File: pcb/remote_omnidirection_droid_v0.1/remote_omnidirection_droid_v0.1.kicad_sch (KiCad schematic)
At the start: 30 parts, among them J1 USB_C_Receptacle_USB2.0, J4 Conn_01x02, Q1 BC846BS, SW1 SW_SPST, U1 USBLC6-2SC6, U3 AZ1117-3.3, U4 AZ1117-5.0, U5 ESP32-S3-WROOM-2-N32R8V

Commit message: poorly designed a PCB
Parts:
- C11, C12, C17: footprint (none) -> Capacitor_SMD:C_1206_3216Metric_Pad1.33x1.80mm_HandSolder
- D1, D2, D8, D9: footprint (none) -> LED_SMD:LED_1206_3216Metric_Pad1.42x1.75mm_HandSolder
- D3, D7: footprint (none) -> Diode_SMD:D_1206_3216Metric_Pad1.42x1.75mm_HandSolder
- J4: footprint (none) -> TestPoint:TestPoint_2Pads_Pitch5.08mm_Drill1.3mm
- R10, R11, R5, R6, R7, R8: footprint (none) -> Resistor_SMD:R_1206_3216Metric_Pad1.30x1.75mm_HandSolder
- U5: footprint ESP32-S3-WROOM-2-N32R8V:XCVR_ESP32-S3-WROOM-2-N32R8V -> ESP32 S3:XCVR_ESP32-S3-WROOM-2-N32R8V
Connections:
- net IO0: no longer names the net of U5.27 (IO0)
- no-connect marks 7 -> 33
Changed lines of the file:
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@@
   (junction (at 56.515 132.715) (diameter 0) (color 0 0 0 0)
   )
+  (no_connect (at 165.1 160.02))
+  (no_connect (at 195.58 167.64))
+  (no_connect (at 195.58 165.1))
+  (no_connect (at 195.58 157.48))
+  (no_connect (at 165.1 162.56))
+  (no_connect (at 165.1 167.64))
   (no_connect (at 165.1 137.16))
+  (no_connect (at 165.1 147.32))
+  (no_connect (at 195.58 162.56))
+  (no_connect (at 165.1 144.78))
+  (no_connect (at 165.1 180.34))
+  (no_connect (at 195.58 142.24))
+  (no_connect (at 165.1 177.8))
+  (no_connect (at 195.58 170.18))
   (no_connect (at 64.135 75.565))
+  (no_connect (at 195.58 147.32))
   (no_connect (at 195.58 175.26))
+  (no_connect (at 165.1 152.4))
+  (no_connect (at 195.58 144.78))
+  (no_connect (at 165.1 170.18))
   (no_connect (at 195.58 177.8))
   (no_connect (at 165.1 134.62))
+  (no_connect (at 165.1 175.26))
+  (no_connect (at 195.58 160.02))
+  (no_connect (at 195.58 154.94))
+  (no_connect (at 165.1 172.72))
   (no_connect (at 165.1 149.86))
+  (no_connect (at 195.58 172.72))
+  (no_connect (at 165.1 154.94))
+  (no_connect (at 165.1 157.48))
   (no_connect (at 64.135 73.025))
+  (no_connect (at 165.1 142.24))
+  (no_connect (at 165.1 165.1))
   (wire (pts (xy 83.185 187.325) (xy 94.615 187.325))
     (stroke (width 0) (type default))
@@
     (stroke (width 0) (type default))
   )
-  (wire (pts (xy 161.29 142.24) (xy 165.1 142.24))
-    (stroke (width 0) (type default))
-  )
   (wire (pts (xy 31.75 215.9) (xy 38.735 215.9))
     (stroke (width 0) (type default))
@@
     (stroke (width 0) (type default))
   )
-  (text_box "ESP32-S3-WROOM Module"
-    (at 125.095 98.425 0) (size 111.125 106.045)
+  (text_box "Enable/Reset Switch"
+    (at 13.335 204.47 0) (size 45.72 27.305)
     (stroke (width 0) (type default))
     (fill (type none))
     (effects (font (size 1.27 1.27)) (justify left top))
   )
-  (text_box "Enable/Reset Switch"
-    (at 13.335 204.47 0) (size 45.72 27.305)
+  (text_box "Power Management"
+    (at 13.335 98.425 0) (size 111.76 106.045)
     (stroke (width 0) (type default))
     (fill (type none))
     (effects (font (size 1.27 1.27)) (justify left top))
   )
-  (text_box "Power Management"
-    (at 13.335 98.425 0) (size 111.76 106.045)
+  (text_box "USB-C + ESD Protection"
+    (at 13.335 34.29 0) (size 111.76 64.135)
     (stroke (width 0) (type default))
     (fill (type none))
     (effects (font (size 1.27 1.27)) (justify left top))
   )
-  (text_box "USB-C + ESD Protection"
-    (at 13.335 34.29 0) (size 111.76 64.135)
+  (text_box "Power Flags"
+    (at 13.335 13.335 0) (size 111.76 20.955)
     (stroke (width 0) (type default))
     (fill (type none))
     (effects (font (size 1.27 1.27)) (justify left top))
   )
-  (text_box "Power Flags"
-    (at 13.335 13.335 0) (size 111.76 20.955)
-    (stroke (width 0) (type default))
-    (fill (type none))
-    (effects (font (size 1.27 1.27)) (justify left top))
-  )
   (label "LED_BATT" (at 83.185 187.325 0) (fields_autoplaced)
     (effects (font (size 1.27 1.27)) (justify left bottom))
@@
     (effects (font (size 1.27 1.27)) (justify left bottom))
   )
-  (label "IO0" (at 161.29 142.24 0) (fields_autoplaced)
-    (effects (font (size 1.27 1.27)) (justify left bottom))
-  )
   (label "EN" (at 52.705 215.9 180) (fields_autoplaced)
     (effects (font (size 1.27 1.27)) (justify right bottom))
@@
       (effects (font (size 1.27 1.27)))
     )
-    (property "Footprint" "ESP32-S3-WROOM-2-N32R8V:XCVR_ESP32-S3-WROOM-2-N32R8V" (at 180.34 157.48 0)
+    (property "Footprint" "ESP32 S3:XCVR_ESP32-S3-WROOM-2-N32R8V" (at 180.34 157.48 0)
       (effects (font (size 1.27 1.27)) (justify bottom) hide)
     )
@@
       (effects (font (size 1.27 1.27)))
     )
-    (property "Footprint" "" (at 81.915 164.465 0)
+    (property "Footprint" "Resistor_SMD:R_1206_3216Metric_Pad1.30x1.75mm_HandSolder" (at 81.915 164.465 0)
       (effects (font (size 1.27 1.27)) hide)
     )
@@
       (effects (font (size 1.27 1.27)))
     )
-    (property "Footprint" "" (at 93.345 158.115 0)
+    (property "Footprint" "LED_SMD:LED_1206_3216Metric_Pad1.42x1.75mm_HandSolder" (at 93.345 158.115 0)
       (effects (font (size 1.27 1.27)) hide)
     )
@@
       (effects (font (size 1.27 1.27)))
     )
-    (property "Footprint" "" (at 30.48 132.715 0)
+    (property "Footprint" "Diode_SMD:D_1206_3216Metric_Pad1.42x1.75mm_HandSolder" (at 30.48 132.715 0)
       (effects (font (size 1.27 1.27)) hide)
     )
@@
       (effects (font (size 1.27 1.27)))
     )
-    (property "Footprint" "" (at 81.915 151.765 0)
+    (property "Footprint" "Resistor_SMD:R_1206_3216Metric_Pad1.30x1.75mm_HandSolder" (at 81.915 151.765 0)
       (effects (font (size 1.27 1.27)) hide)
     )
@@
       (effects (font (size 1.27 1.27)))
     )
-    (property "Footprint" "" (at 62.23 132.715 0)
+    (property "Footprint" "Diode_SMD:D_1206_3216Metric_Pad1.42x1.75mm_HandSolder" (at 62.23 132.715 0)
       (effects (font (size 1.27 1.27)) hide)
     )
@@
       (effects (font (size 1.27 1.27)))
     )
-    (property "Footprint" "" (at 93.345 145.415 0)
+    (property "Footprint" "LED_SMD:LED_1206_3216Metric_Pad1.42x1.75mm_HandSolder" (at 93.345 145.415 0)
       (effects (font (size 1.27 1.27)) hide)
     )
@@
       (effects (font (size 1.27 1.27)))
     )
-    (property "Footprint" "" (at 180.34 114.3 0)
+    (property "Footprint" "Resistor_SMD:R_1206_3216Metric_Pad1.30x1.75mm_HandSolder" (at 180.34 114.3 0)
       (effects (font (size 1.27 1.27)) hide)
     )
@@
       (effects (font (size 1.27 1.27)) (justify left))
     )
-    (property "Footprint" "" (at 102.235 187.325 0)
+    (property "Footprint" "TestPoint:TestPoint_2Pads_Pitch5.08mm_Drill1.3mm" (at 102.235 187.325 0)
       (effects (font (size 1.27 1.27)) hide)
     )
@@
       (effects (font (size 1.27 1.27)))
     )
-    (property "Footprint" "" (at 81.915 145.415 0)
+    (property "Footprint" "Resistor_SMD:R_1206_3216Metric_Pad1.30x1.75mm_HandSolder" (at 81.915 145.415 0)
       (effects (font (size 1.27 1.27)) hide)
     )
@@
       (effects (font (size 1.27 1.27)) (justify left))
     )
-    (property "Footprint" "" (at 207.01 131.445 0)
+    (property "Footprint" "Capacitor_SMD:C_1206_3216Metric_Pad1.33x1.80mm_HandSolder" (at 207.01 131.445 0)
       (effects (font (size 1.27 1.27)) hide)
     )
@@
       (effects (font (size 1.27 1.27)))
     )
-    (property "Footprint" "" (at 93.345 151.765 0)
+    (property "Footprint" "LED_SMD:LED_1206_3216Metric_Pad1.42x1.75mm_HandSolder" (at 93.345 151.765 0)
       (effects (font (size 1.27 1.27)) hide)
     )
@@
       (effects (font (size 1.27 1.27)) (justify left))
     )
-    (property "Footprint" "" (at 215.265 131.445 0)
+    (property "Footprint" "Capacitor_SMD:C_1206_3216Metric_Pad1.33x1.80mm_HandSolder" (at 215.265 131.445 0)
       (effects (font (size 1.27 1.27)) hide)
     )
@@
       (effects (font (size 1.27 1.27)))
     )
-    (property "Footprint" "" (at 41.91 107.315 0)
+    (property "Footprint" "Resistor_SMD:R_1206_3216Metric_Pad1.30x1.75mm_HandSolder" (at 41.91 107.315 0)
       (effects (font (size 1.27 1.27)) hide)
     )
@@
       (effects (font (size 1.27 1.27)))
     )
-    (property "Footprint" "" (at 93.345 164.465 0)
+    (property "Footprint" "LED_SMD:LED_1206_3216Metric_Pad1.42x1.75mm_HandSolder" (at 93.345 164.465 0)
       (effects (font (size 1.27 1.27)) hide)
     )
@@
       (effects (font (size 1.27 1.27)) (justify left))
     )
-    (property "Footprint" "" (at 39.37 125.095 0)
+    (property "Footprint" "Capacitor_SMD:C_1206_3216Metric_Pad1.33x1.80mm_HandSolder" (at 39.37 125.095 0)
       (effects (font (size 1.27 1.27)) hide)
     )
@@
       (effects (font (size 1.27 1.27)))
     )
-    (property "Footprint" "" (at 81.915 158.115 0)
-      (effects (font (size 1.27 1.27)) hide)
-    )
+    (property "Footprint" "Resistor_SMD:R_1206_3216Metric_Pad1.30x1.75mm_HandSolder" (at 81.915 158.115 0)
+      (effects (font (size 1.27 1.27)) hide)
+    )

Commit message: updated PCB
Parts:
- added C4: 0.1u, Capacitor_SMD:C_1206_3216Metric_Pad1.33x1.80mm_HandSolder, symbol Device:C_Small
- added J2, J4, J5: Conn_01x04, Connector_PinSocket_2.54mm:PinSocket_1x04_P2.54mm_Vertical_SMD_Pin1Left, symbol Connector_Generic:Conn_01x04
- added M1, M2, M3: Motor_DC_ALT, pimoroni_motor_breakout:Pimoroni_Motor_Breakout, symbol Motor:Motor_DC_ALT
- added R10, R11, R12, R13, R7, R8: 10k, Resistor_SMD:R_1206_3216Metric_Pad1.30x1.75mm_HandSolder, symbol Device:R_Small_US
- added SW2: SW_SPST, Button_Switch_SMD:SW_Tactile_SPST_NO_Straight_CK_PTS636Sx25SMTRLFS, symbol Switch:SW_SPST
- added SW3: SW_SPDT, myparts:SWITCH_25336NA_APM, symbol Switch:SW_SPDT
- added TP1: AMMETER_CONN, TestPoint:TestPoint_2Pads_Pitch5.08mm_Drill1.3mm, symbol Connector:TestPoint_2Pole
- J3: renamed from J4; value Conn_01x02 -> BATT_CONNECT; footprint TestPoint:TestPoint_2Pads_Pitch5.08mm_Drill1.3mm -> myparts:Deans T-Plug Header
- renumbered C7 to C1, C9 to C2, C14 to C3, C17 to C5, C8 to C6, C10 to C7, C12 to C8, C11 to C9, D3 to D1, D8 to D3, D9 to D4, D7 to D5, D1 to D6, R10 to R14, R11 to R3, R6 to R4, R7 to R5, R8 to R6, R5 to R9, U3 to U1, U4 to U2, U1 to U3, U5 to U4
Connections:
- net +3V3: now also R4.1; no longer R5.1
- net +5V: now also R5.1, J2.1 (Pin_1), J4.1 (Pin_1), J5.1 (Pin_1); no longer R4.1
- net +BATT: now also SW3.3 (C), TP1.1; no longer J3.1 (Pin_1)
- net GND: now also C4.2, J2.4 (Pin_4), J4.4 (Pin_4), J5.4 (Pin_4), R11.2, R13.2, R8.2, SW2.1 (A)
- net BOOT: now reaches U4.27 (IO0)
- net BOOT: now also C4.1, SW2.2 (B)
- net CC1: now reaches J1.A5 (CC1), R2.2
- net NESD_D+: now reaches J1.A6 (D+), J1.B6 (D+), U3.1 (I/O1)
- net NESD_D-: now reaches J1.A7 (D-), J1.B7 (D-), U3.3 (I/O2)
- net CC2: now reaches J1.B5 (CC2), R1.2
- net LED_USB: no longer names the net of C5.2, D1.1 (K), D5.2 (A), Q1.2 (B1), R3.2, R6.1
- new net: J5.3 (Pin_3), R12.2, R13.1
- new net: J4.3 (Pin_3), R10.2, R11.1
- new net: SW3.1 (A), TP1.2
- new net: J3.1 (Pin_1), SW3.2 (B)
- new net: J2.3 (Pin_3), R7.2, R8.1
- new net ECHO1: R7.1
- new net ECHO2: R10.1
- new net ECHO3: R12.1
- new net TRIG1: J2.2 (Pin_2)
- new net TRIG2: J4.2 (Pin_2)
- new net TRIG3: J5.2 (Pin_2)
- no-connect marks 33 -> 38
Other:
- moved on the sheet: C2, C7, D2, D3, D4, D6, J3, R4, R5, R6, R9, U2

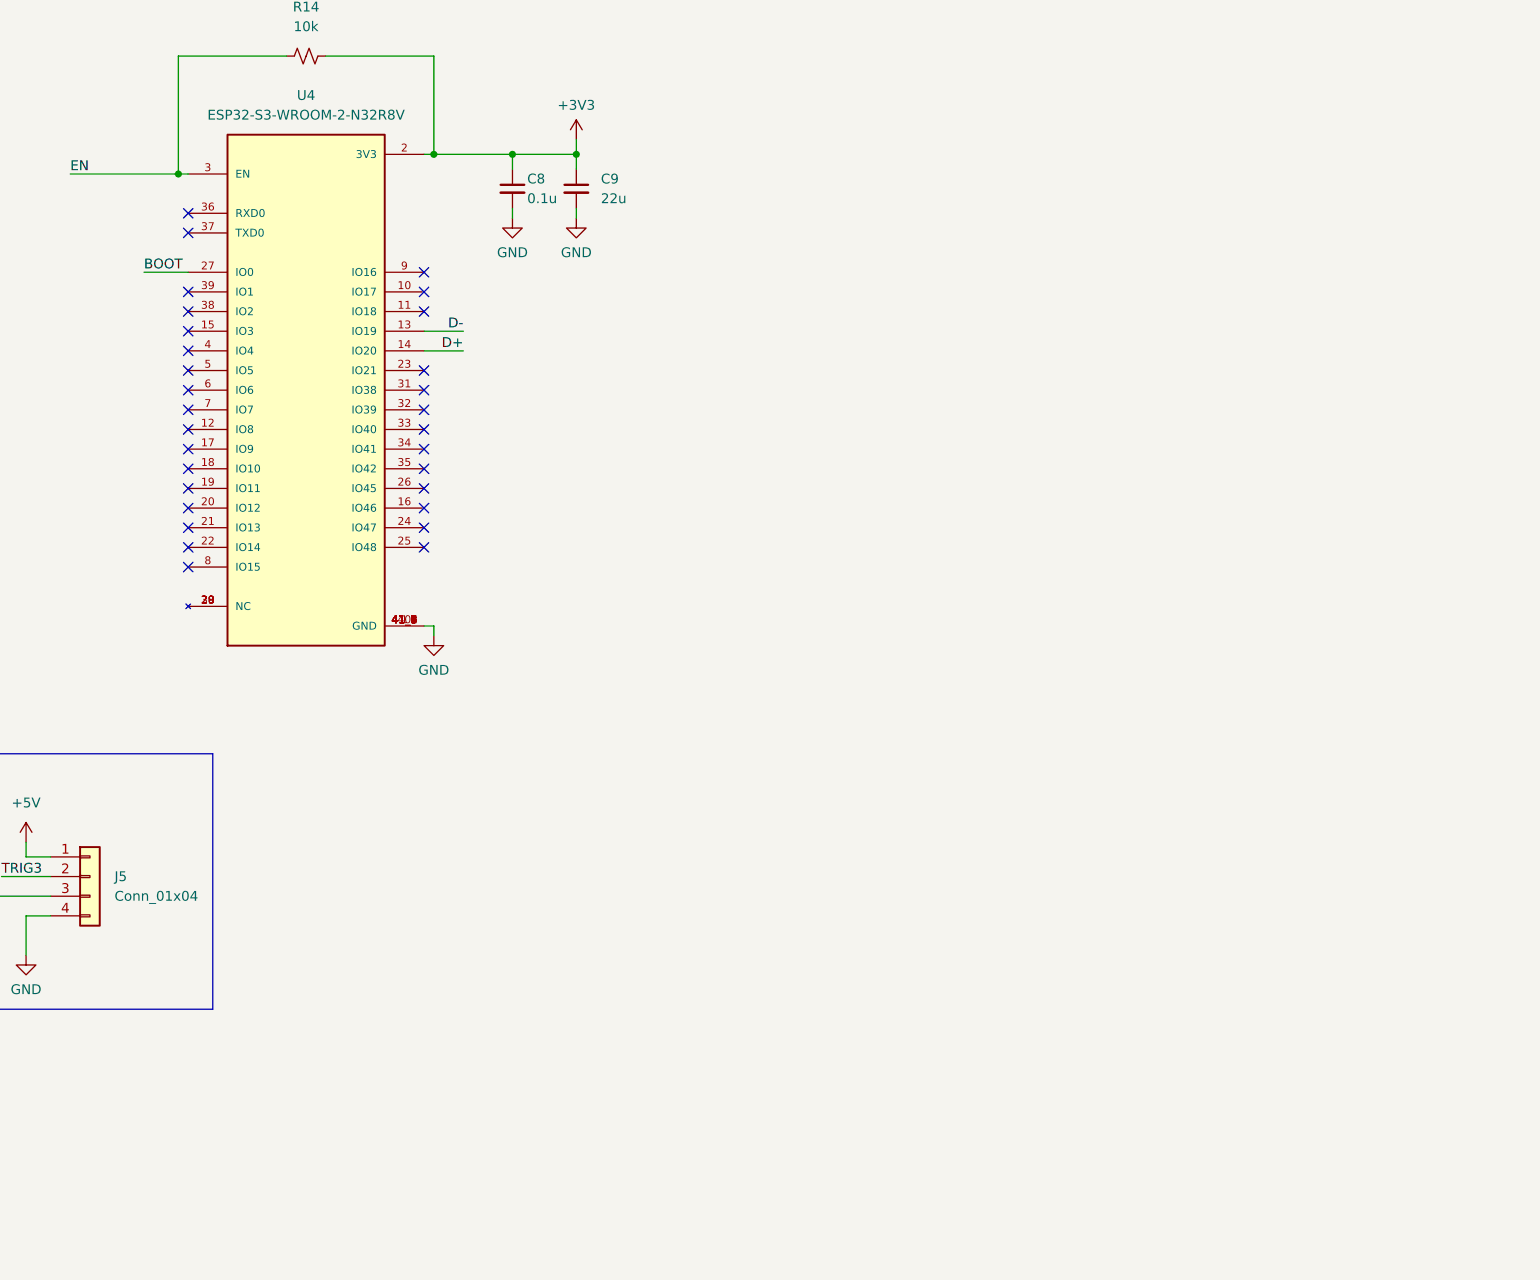
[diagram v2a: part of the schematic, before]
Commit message: started adding MOTOR DRIVERS
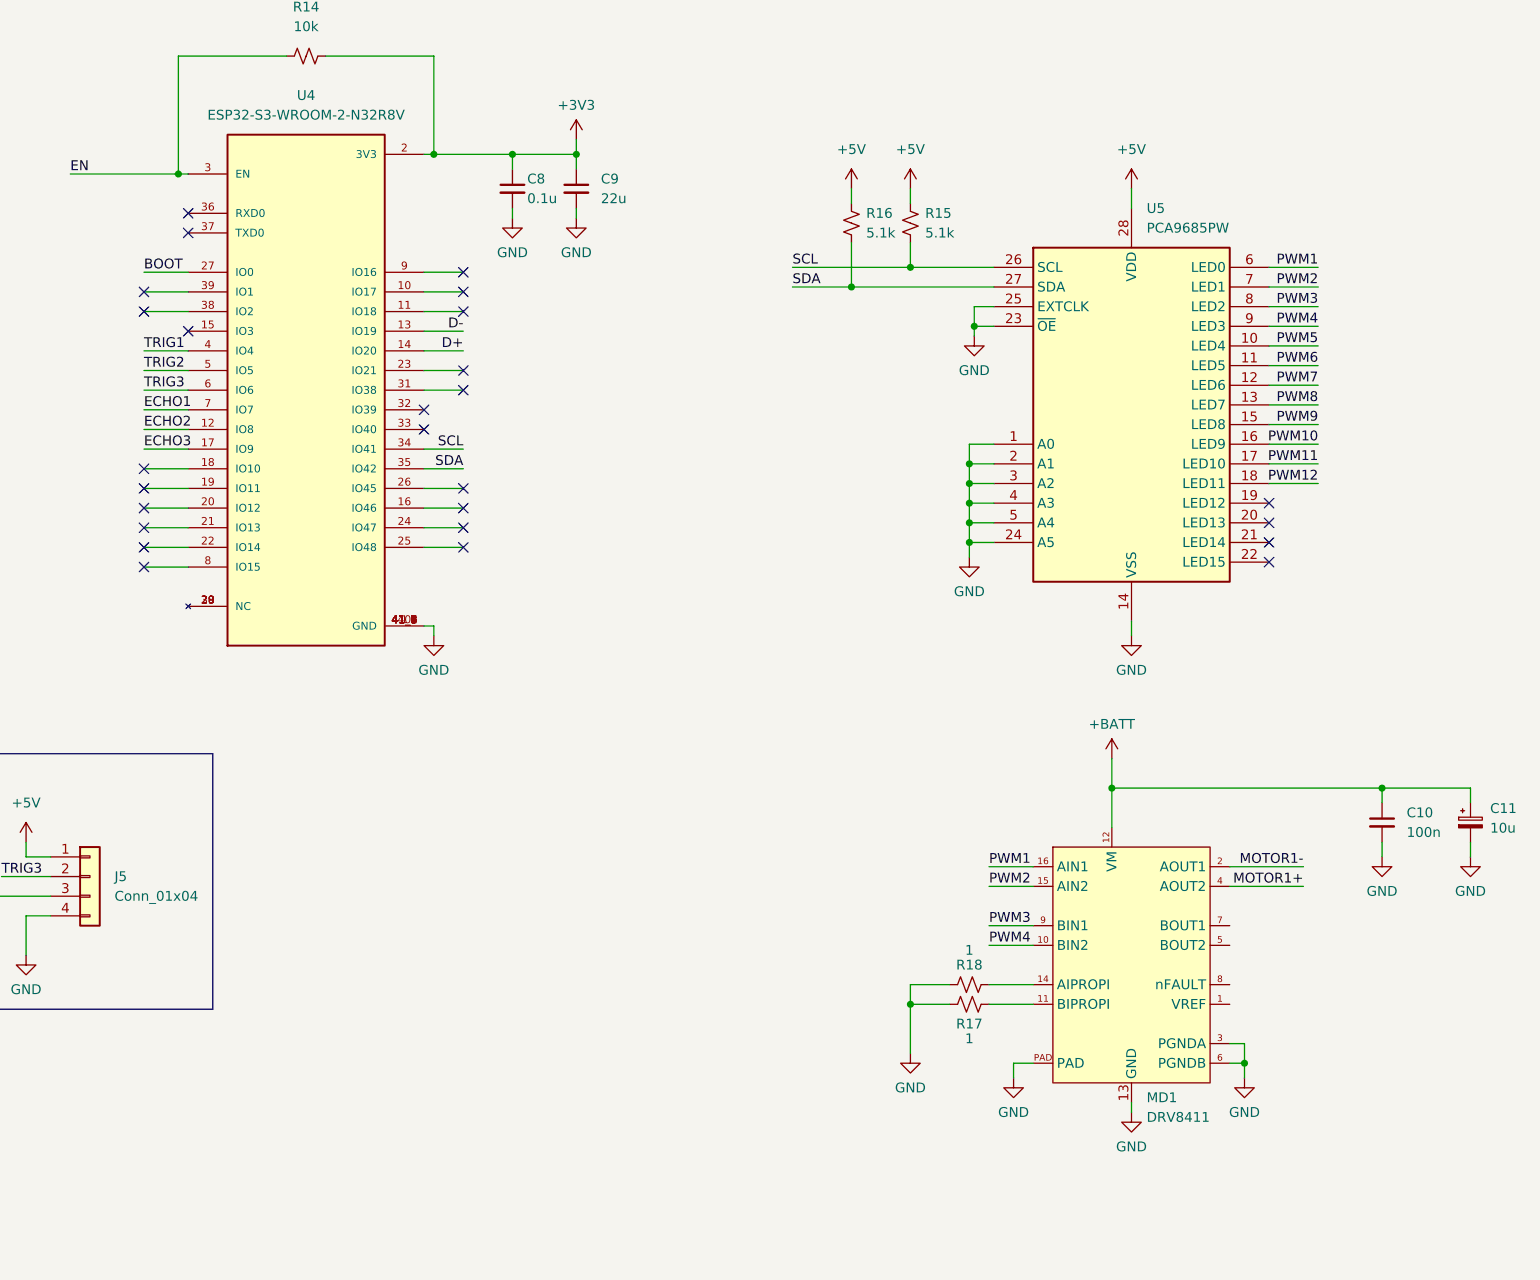
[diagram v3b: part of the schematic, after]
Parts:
- added C10: 100n, symbol Device:C_Small
- added C11: 10u, symbol Device:C_Polarized_Small
- added MD1: DRV8411, symbol DroidSymbols:DRV8411
- added R15, R16: 5.1k, symbol Device:R_Small_US
- added R17, R18: 1, symbol Device:R_Small_US
- added U5: PCA9685PW, Package_SO:TSSOP-28_4.4x9.7mm_P0.65mm, symbol Driver_LED:PCA9685PW
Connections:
- net +5V: now also R15.1, R16.1, U5.28 (VDD)
- net +BATT: now also C10.1, C11.1, MD1.12 (VM)
- net ECHO1: now also U4.7 (IO7)
- net ECHO2: now also U4.12 (IO8)
- net ECHO3: now also U4.17 (IO9)
- net GND: now also C10.2, C11.2, MD1.13 (GND), MD1.3 (PGNDA), MD1.6 (PGNDB), MD1.PAD, R17.2, R18.2, U5.1 (A0), U5.14 (VSS), U5.2 (A1), U5.23 (~{OE}), U5.24 (A5), U5.25 (EXTCLK), U5.3 (A2), U5.4 (A3), U5.5 (A4)
- net TRIG1: now also U4.4 (IO4)
- net TRIG2: now also U4.5 (IO5)
- net TRIG3: now also U4.6 (IO6)
- net SCL: now reaches U4.34 (IO41)
- net SCL: now also R15.2, U5.26 (SCL)
- net SDA: now reaches U4.35 (IO42)
- net SDA: now also R16.2, U5.27 (SDA)
- new net: MD1.11 (BIPROPI), R17.1
- new net: MD1.14 (AIPROPI), R18.1
- new net MOTOR1+: MD1.4 (AOUT2)
- new net MOTOR1-: MD1.2 (AOUT1)
- new net PWM1: MD1.16 (AIN1), U5.6 (LED0)
- new net PWM10: U5.16 (LED9)
- new net PWM11: U5.17 (LED10)
- new net PWM12: U5.18 (LED11)
- new net PWM2: MD1.15 (AIN2), U5.7 (LED1)
- new net PWM3: MD1.9 (BIN1), U5.8 (LED2)
- new net PWM4: MD1.10 (BIN2), U5.9 (LED3)
- new net PWM5: U5.10 (LED4)
- new net PWM6: U5.11 (LED5)
- new net PWM7: U5.12 (LED6)
- new net PWM8: U5.13 (LED7)
- new net PWM9: U5.15 (LED8)
- no-connect marks 38 -> 34
